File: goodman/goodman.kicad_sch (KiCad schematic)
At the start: 13 parts, among them J1 TSM-110-01-T-DV, Q1 BSS138BKT116, U1 LP5907MFX-3.3/NOPB, U2 REF3425IDBVR, U3 TPS62821DLCR

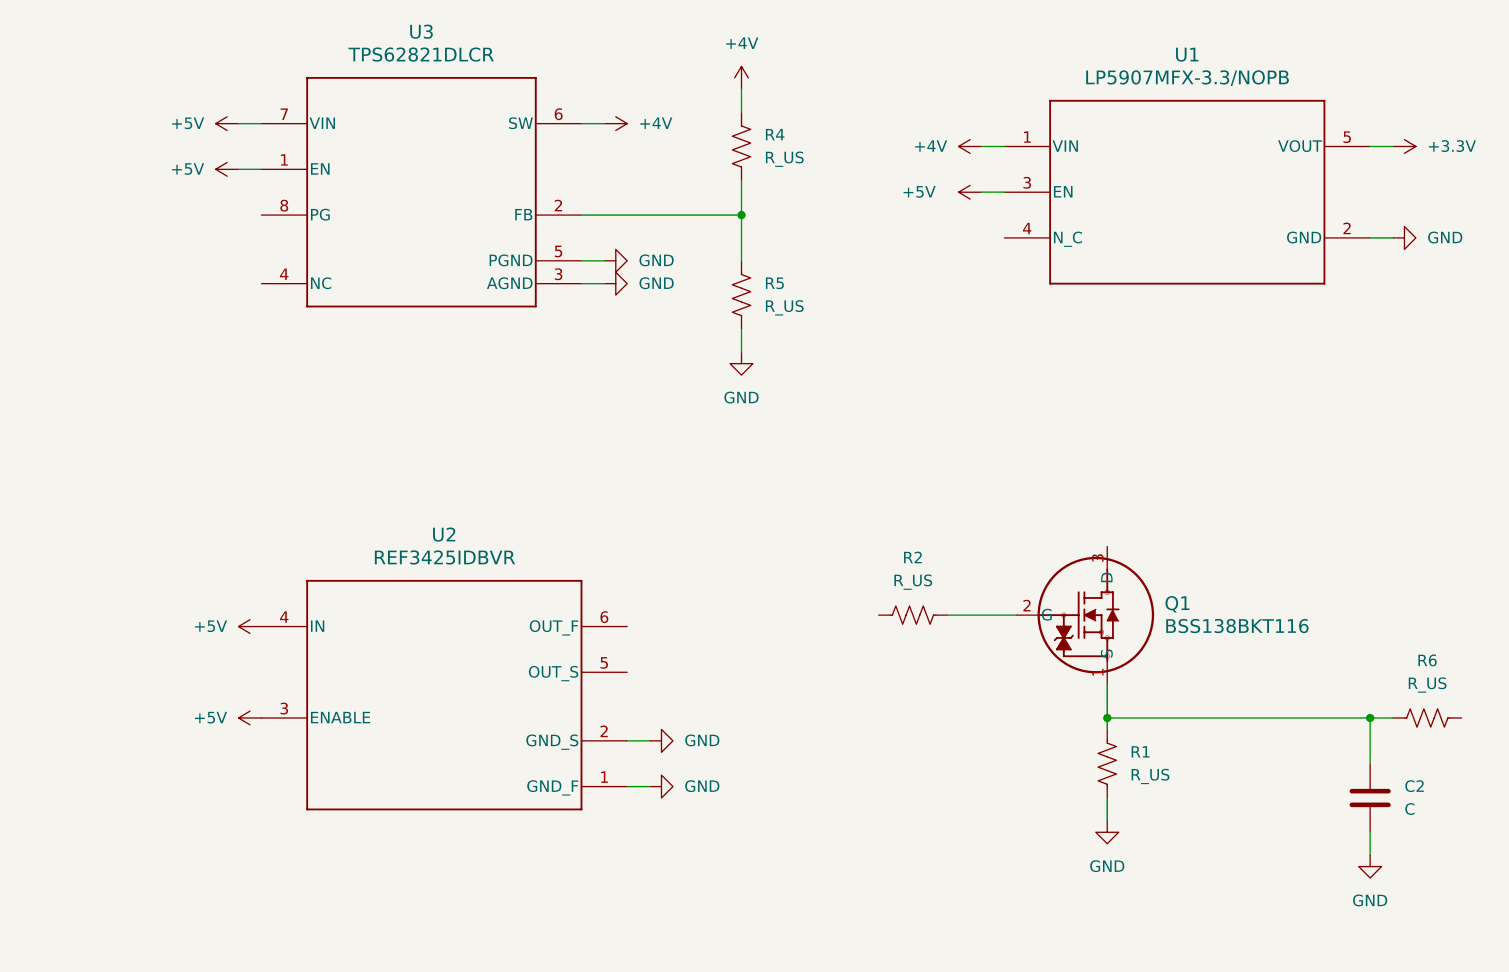
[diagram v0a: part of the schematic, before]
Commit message: Removed hardware not needed for carrier board.
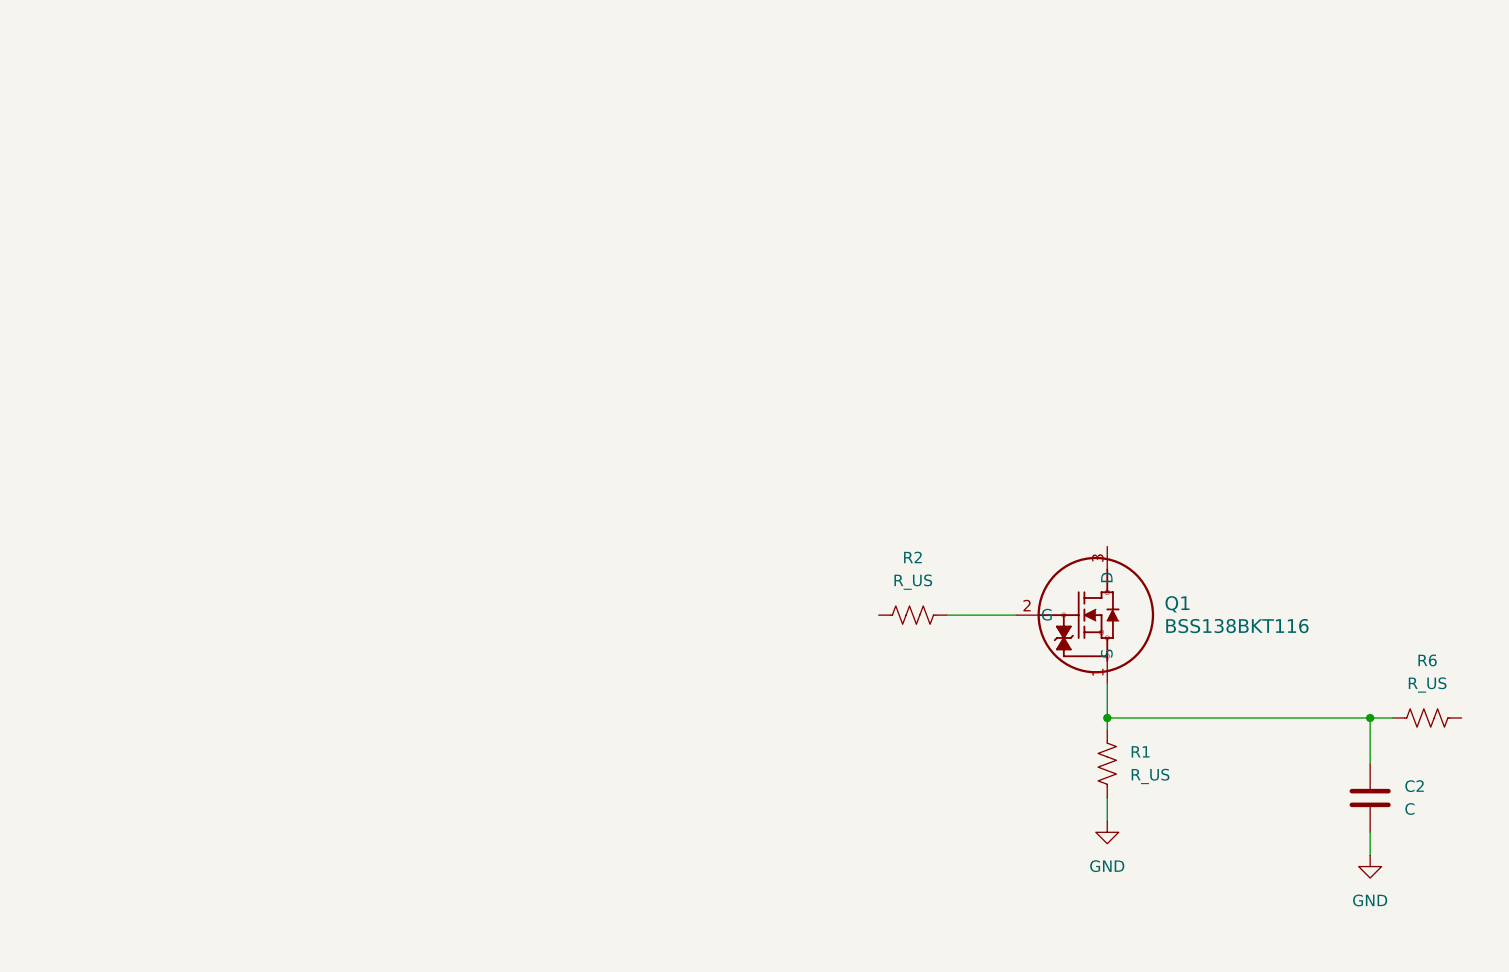
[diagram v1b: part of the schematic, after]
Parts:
- removed R4, R5: R_US, symbol Device:R_US
- removed U1: LP5907MFX-3.3/NOPB, DBV0005A_N, symbol Goodman Local:LP5907MFX-3.3_NOPB
- removed U2: REF3425IDBVR, DBV0006A_N, symbol Goodman Local:REF3425IDBVR
- removed U3: TPS62821DLCR, DLC0008A, symbol Goodman Local:TPS62821DLCR

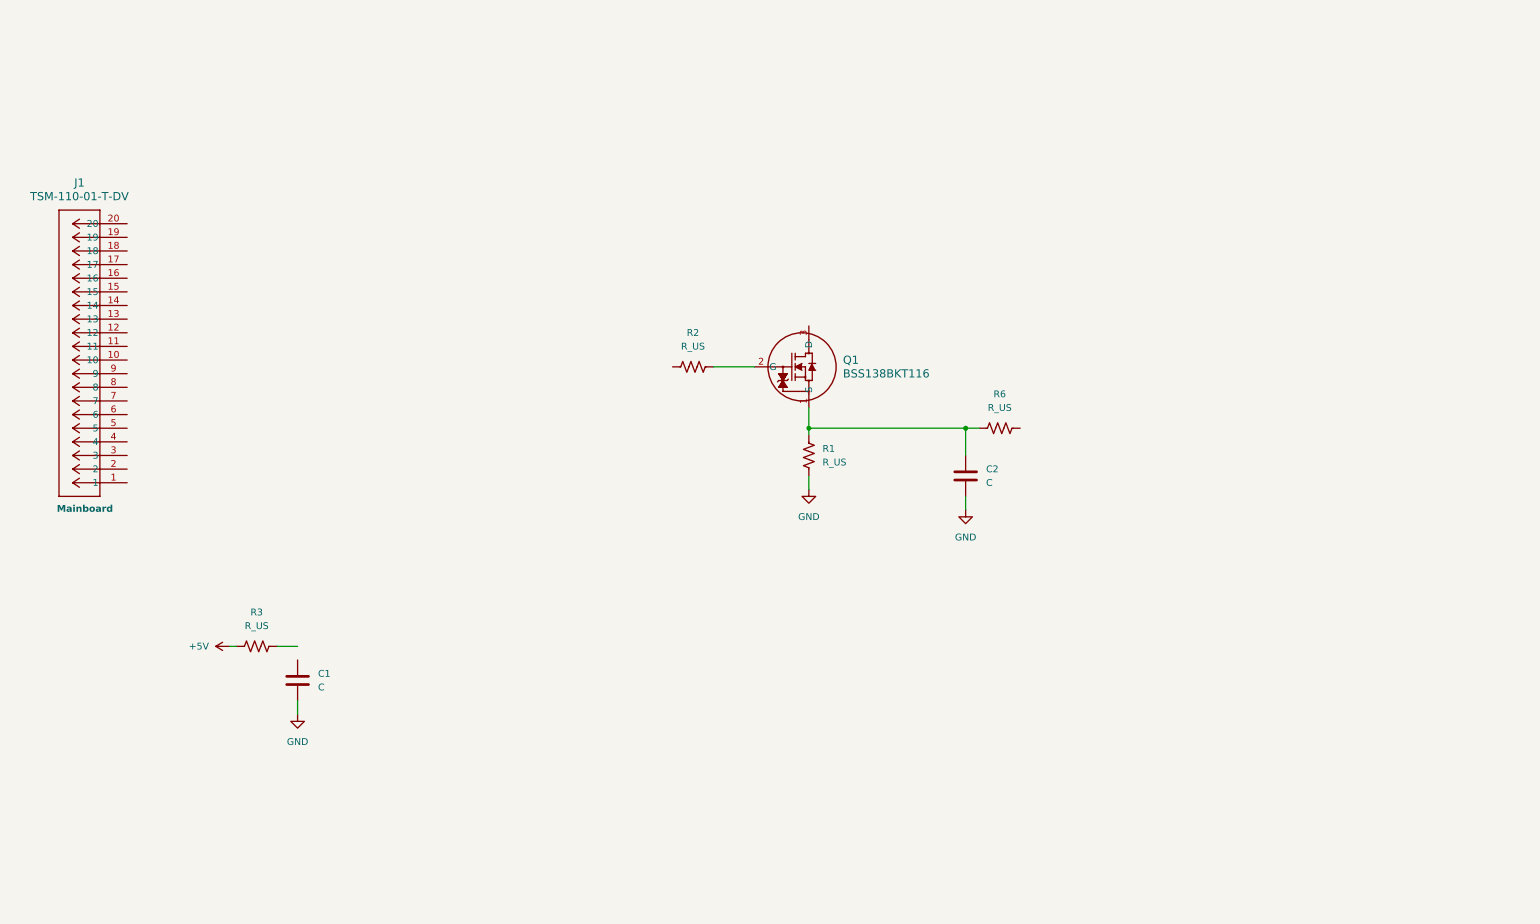
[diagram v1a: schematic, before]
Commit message: Fixed ADC1256 wiring organization.
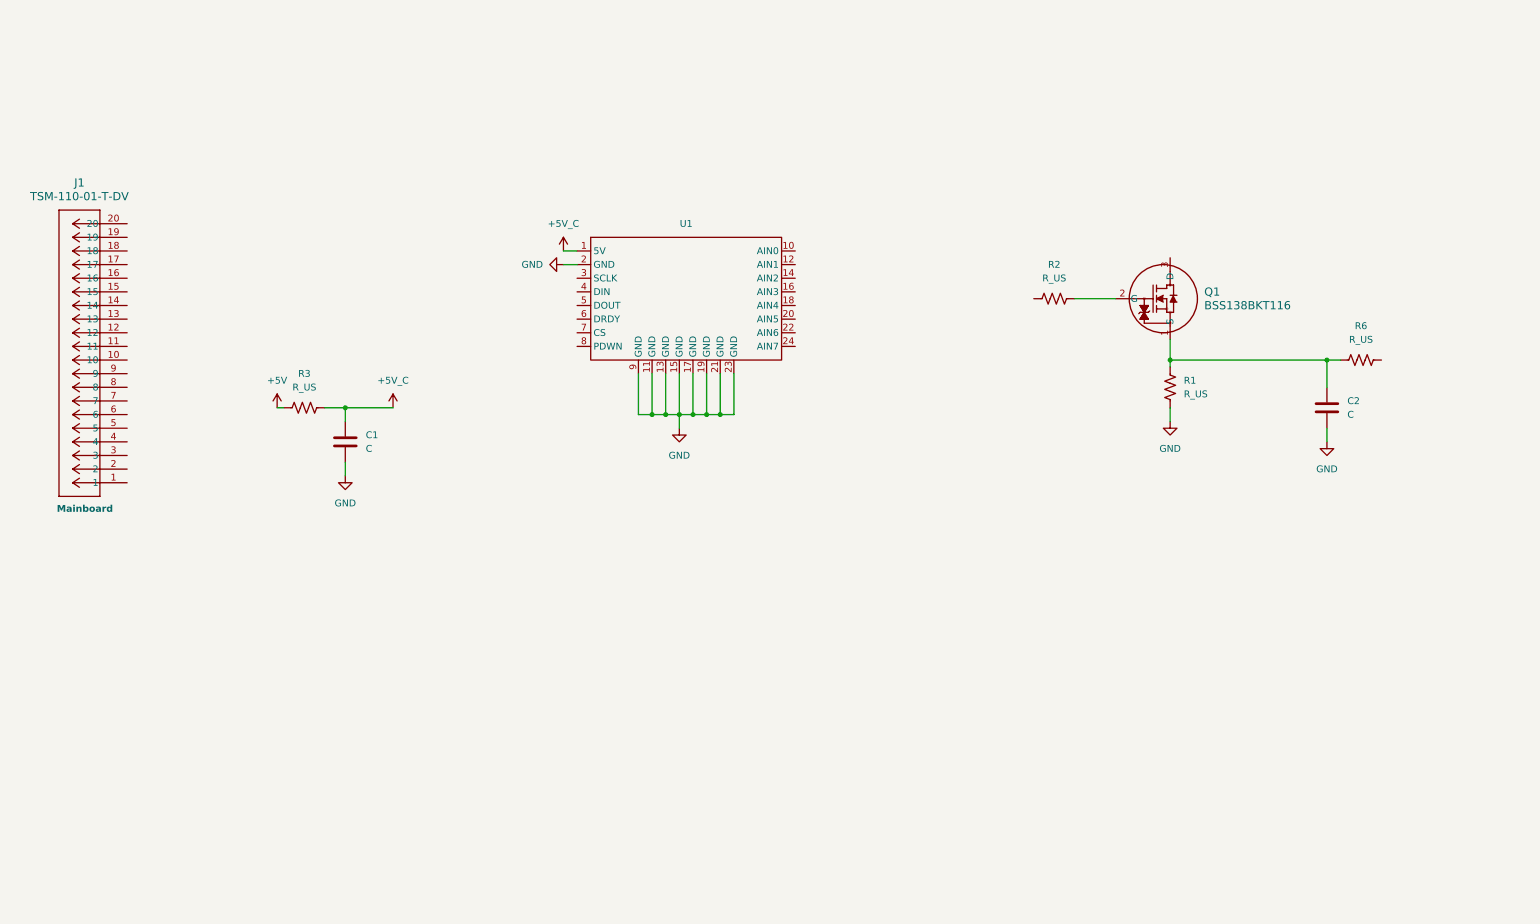
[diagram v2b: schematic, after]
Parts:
- added U1: (no value), symbol Goodman Local:HiLetgo_ADS1256
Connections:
- net GND: now also U1.11 (GND), U1.13 (GND), U1.15 (GND), U1.17 (GND), U1.19 (GND), U1.2 (GND), U1.21 (GND), U1.23 (GND), U1.9 (GND)
- net +5V_C: now reaches C1.1
- net +5V_C: now also R3.2, U1.1 (5V)
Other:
- moved on the sheet: C1, C2, Q1, R1, R2, R3, R6

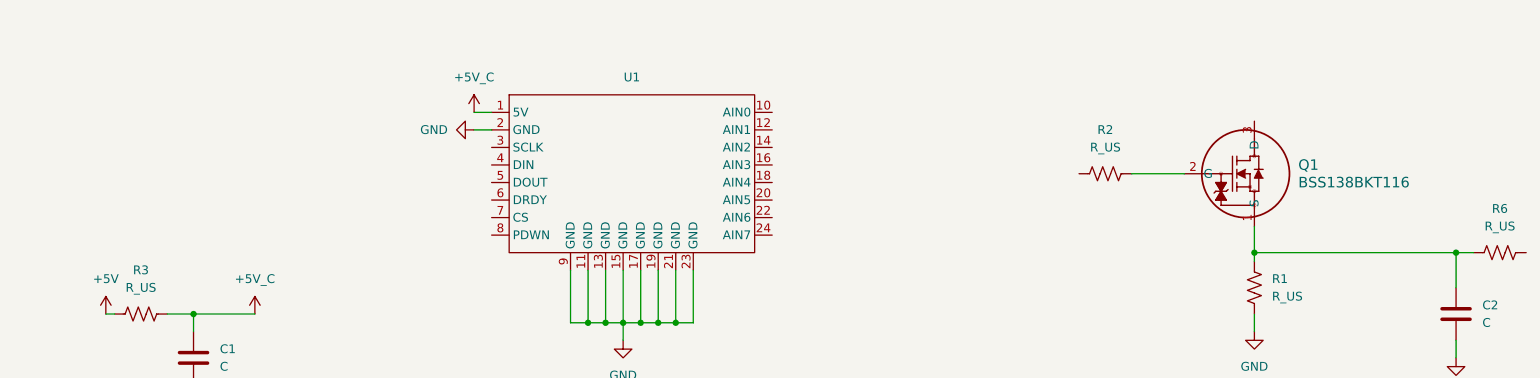
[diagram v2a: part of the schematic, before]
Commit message: Added Labels for Filters.
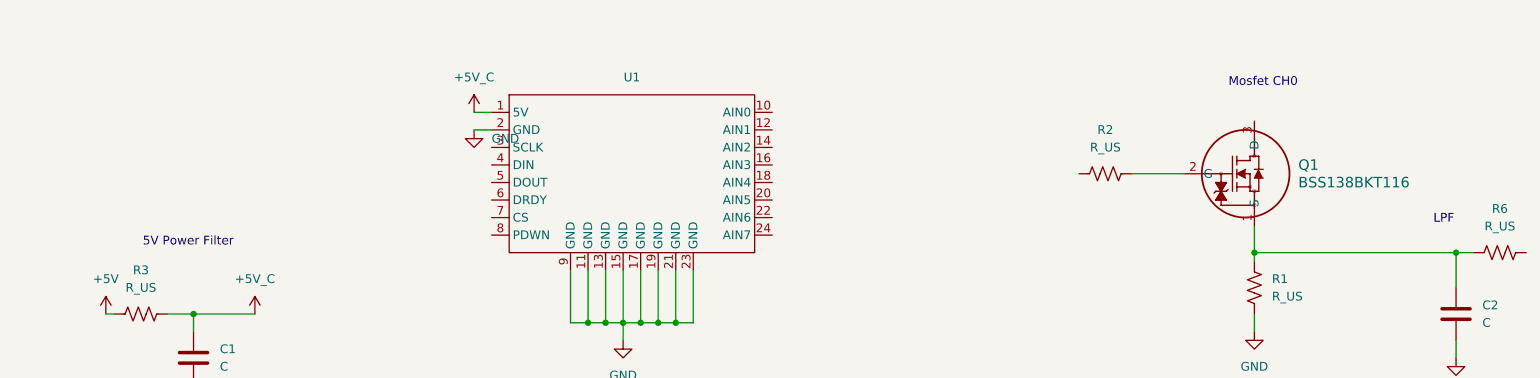
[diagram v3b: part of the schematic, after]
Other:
- note added: "5V Power Filter"
- note added: "LPF"
- note added: "Mosfet CH0"
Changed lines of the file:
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@@
 	(generator_version "10.0")
 	(paper "A4")
+	(text "LPF"
+		(exclude_from_sim no)
+		(at 256.032 81.534 0)
+		(effects
+			(font
+				(size 1.27 1.27)
+			)
+		)
+	)
+	(text "5V Power Filter"
+		(exclude_from_sim no)
+		(at 74.168 84.836 0)
+		(effects
+			(font
+				(size 1.27 1.27)
+			)
+		)
+	)
+	(text "Mosfet CH0"
+		(exclude_from_sim no)
+		(at 229.87 61.722 0)
+		(effects
+			(font
+				(size 1.27 1.27)
+			)
+		)
+	)
 	(junction
 		(at 134.62 96.52)
@@
 	(symbol
 		(lib_id "power:GND")
-		(at 115.57 68.58 270)
+		(at 115.57 68.58 0)
 		(unit 1)
 		(body_style 1)
@@
 		(fields_autoplaced yes)
 		(property "Reference" "#PWR03"
-			(at 109.22 68.58 0)
+			(at 115.57 74.93 0)
 			(hide yes)
 			(show_name no)
@@
 		)
 		(property "Value" "GND"
-			(at 111.76 68.5799 90)
-			(show_name no)
-			(do_not_autoplace no)
-			(effects
-				(font
-					(size 1.27 1.27)
-				)
-				(justify right)
-			)
-		)
+			(at 118.11 69.8499 0)
+			(show_name no)
+			(do_not_autoplace no)
+			(effects
+				(font
+					(size 1.27 1.27)
+				)
+				(justify left)
+			)
+		)

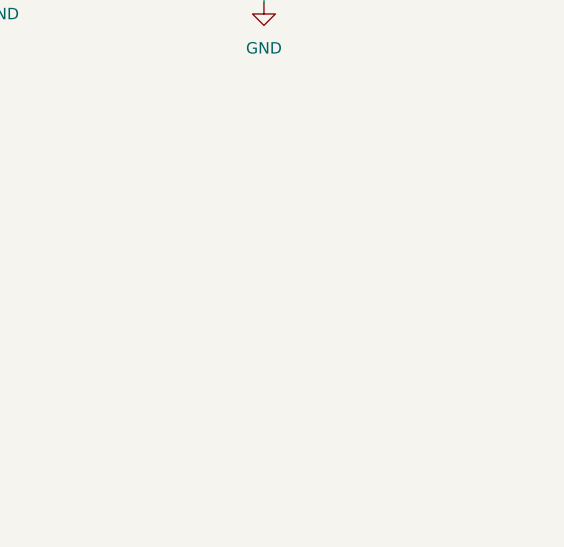
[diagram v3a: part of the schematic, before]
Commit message: Added D-SUB connector
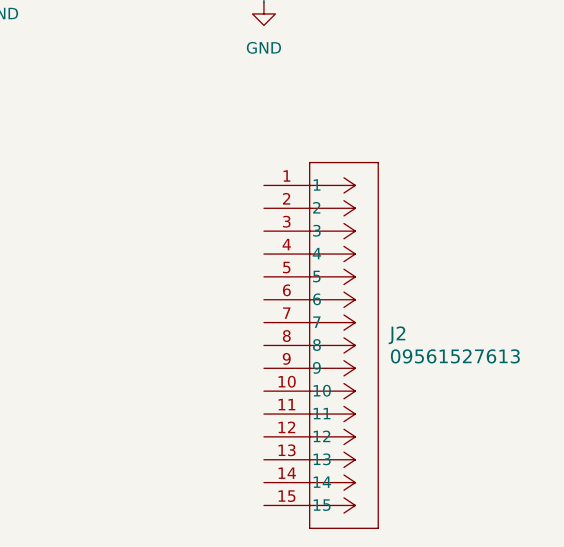
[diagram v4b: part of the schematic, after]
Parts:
- added J2: 09561527613, CONN_09561527613_HAR, symbol Goodman Local:09561527613
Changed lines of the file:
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@@
+	)
+	(symbol
+		(lib_id "Goodman Local:09561527613")
+		(at 257.81 121.92 0)
+		(unit 1)
+		(body_style 1)
+		(exclude_from_sim no)
+		(in_bom yes)
+		(on_board yes)
+		(in_pos_files yes)
+		(dnp no)
+		(fields_autoplaced yes)
+		(property "Reference" "J2"
+			(at 271.78 138.4299 0)
+			(show_name no)
+			(do_not_autoplace no)
+			(effects
+				(font
+					(size 1.524 1.524)
+				)
+				(justify left)
+			)
+		)
+		(property "Value" "09561527613"
+			(at 271.78 140.9699 0)
+			(show_name no)
+			(do_not_autoplace no)
+			(effects
+				(font
+					(size 1.524 1.524)
+				)
+				(justify left)
+			)
+		)
+		(property "Footprint" "CONN_09561527613_HAR"
+			(at 257.81 121.92 0)
+			(hide yes)
+			(show_name no)
+			(do_not_autoplace no)
+			(effects
+				(font
+					(size 1.27 1.27)
+					(italic yes)
+				)
+			)
+		)
+		(property "Datasheet" "09561527613"
+			(at 257.81 121.92 0)
+			(hide yes)
+			(show_name no)
+			(do_not_autoplace no)
+			(effects
+				(font
+					(size 1.27 1.27)
+					(italic yes)
+				)
+			)
+		)
+		(property "Description" ""
+			(at 257.81 121.92 0)
+			(hide yes)
+			(show_name no)
+			(do_not_autoplace no)
+			(effects
+				(font
+					(size 1.27 1.27)
+				)
+			)
+		)
+		(pin "2"
+		)
+		(pin "1"
+		)
+		(pin "10"
+		)
+		(pin "5"
+		)
+		(pin "4"
+		)
+		(pin "8"
+		)
+		(pin "3"
+		)
+		(pin "9"
+		)
+		(pin "6"
+		)
+		(pin "7"
+		)
+		(pin "11"
+		)
+		(pin "14"
+		)
+		(pin "15"
+		)
+		(pin "13"
+		)
+		(pin "12"
+		)
+		(instances
+			(project "goodman"
+				(path "/52ec5281-98f9-4967-92c1-b39f2426ce6f"
+					(reference "J2")
+					(unit 1)
+				)
+			)
+		)
 	)
 	(symbol
